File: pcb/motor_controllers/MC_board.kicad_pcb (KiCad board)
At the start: 2 copper layers, 21 parts, among them U1 Teensy3.2

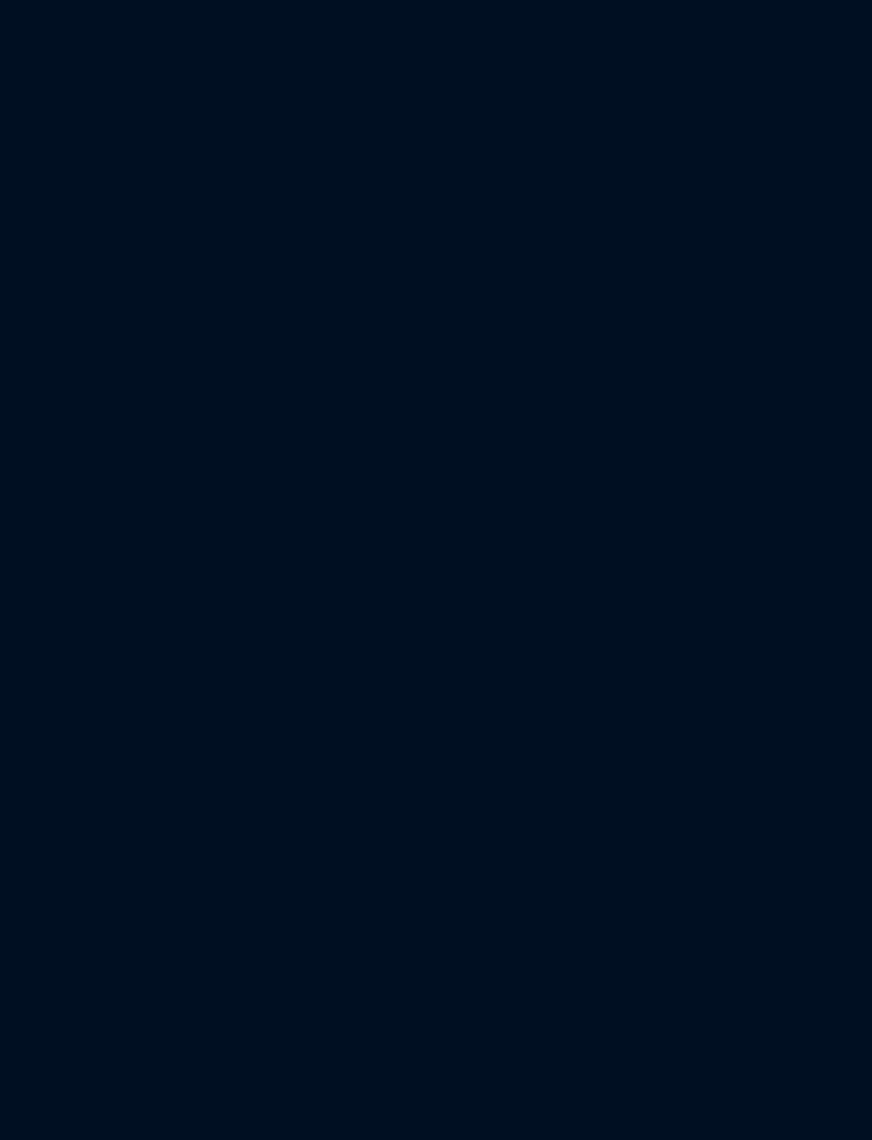
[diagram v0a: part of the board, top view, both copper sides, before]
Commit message: Added analog output RJ45 and audio amplifier symbol.
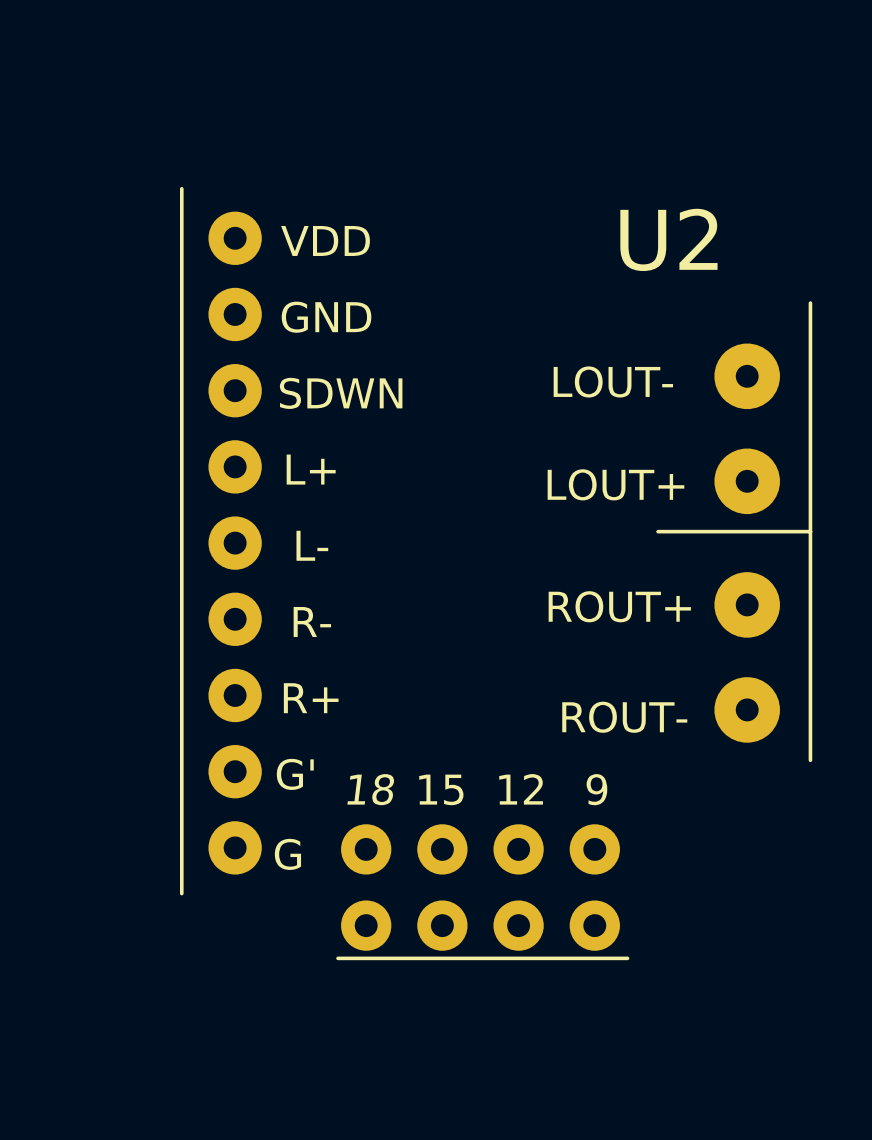
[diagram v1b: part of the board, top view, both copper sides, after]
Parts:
- added U2: MAX98306, spatialsparrow:MAX98306, F.Cu at (149.9, 83.8)
- 5V1: value Barrel_Jack -> 5V
- 9V1: value Barrel_Jack -> 9V
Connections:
- 9V1 pad 1: Net-(9V1-Pad1) -> +9V
- 9V1 pad 2: Net-(9V1-Pad2) -> GND
- C1 pad 1: Net-(9V1-Pad1) -> +9V
- C1 pad 2: Net-(9V1-Pad2) -> GND
- MC-LeverL1 pad 1: Net-(5V1-Pad2) -> GND
- MC-LeverL1 pad 14: Net-(5V1-Pad1) -> +5V
- MC-LeverL1 pad 7: Net-(9V1-Pad2) -> GND
- MC-LeverL1 pad 8: Net-(9V1-Pad1) -> +9V
- MC-LeverR1 pad 1: Net-(5V1-Pad2) -> GND
- MC-LeverR1 pad 14: Net-(5V1-Pad1) -> +5V
- MC-LeverR1 pad 7: Net-(9V1-Pad2) -> GND
- MC-LeverR1 pad 8: Net-(9V1-Pad1) -> +9V
- MC-SpoutL1 pad 1: Net-(5V1-Pad2) -> GND
- MC-SpoutL1 pad 14: Net-(5V1-Pad1) -> +5V
- MC-SpoutL1 pad 7: Net-(9V1-Pad2) -> GND
- MC-SpoutL1 pad 8: Net-(9V1-Pad1) -> +9V
- MC-SpoutR1 pad 1: Net-(5V1-Pad2) -> GND
- MC-SpoutR1 pad 14: Net-(5V1-Pad1) -> +5V
- MC-SpoutR1 pad 7: Net-(9V1-Pad2) -> GND
- MC-SpoutR1 pad 8: Net-(9V1-Pad1) -> +9V
- U1 pad 1: Net-(U1-Pad1) -> GND
- U1 pad 32: Net-(U1-Pad32) -> GND
- U1 pad 33: Net-(U1-Pad33) -> +5V
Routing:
- net Net-(5V1-Pad1): track 1.19 -> 0.00 mm
- net +5V: track 0.00 -> 1.19 mm
- net GND: track 0.00 -> 0.94 mm
- net Net-(9V1-Pad2): track 0.54 -> 0.00 mm

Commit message: ran connections and did board layout
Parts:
- removed 5VGNDTEST1, 5VTEST1, 9VGNDTEST1, 9VTEST1: TestPoint, TestPoint:TestPoint_Plated_Hole_D5.0mm
- removed C2, C3, C4: 100 uF, Capacitor_THT:C_Rect_L7.2mm_W7.2mm_P5.00mm_FKS2_FKP2_MKS2_MKP2
- added 12V1: 12V, Connector_BarrelJack:BarrelJack_Horizontal, F.Cu at (115.6, 54.6)
- added J12V1: Screw_Terminal_01x02, teensey:TerminalBlock_TE_282825-2_1x02_P5.08mm_Horizontal, F.Cu at (108.0, 124.5)
- added J12V2: Screw_Terminal_01x02, teensey:TerminalBlock_TE_282825-2_1x02_P5.08mm_Horizontal, F.Cu at (68.6, 124.5)
- added J12V3: Screw_Terminal_01x02, teensey:TerminalBlock_TE_282825-2_1x02_P5.08mm_Horizontal, F.Cu at (81.3, 124.5)
- added J12V4: Screw_Terminal_01x02, teensey:TerminalBlock_TE_282825-2_1x02_P5.08mm_Horizontal, F.Cu at (94.0, 124.5)
- added J2: RJ45, teensey:RJ45_sparkfun, F.Cu at (113.0, 27.9)
- added J5V1: Screw_Terminal_01x02, teensey:TerminalBlock_TE_282825-2_1x02_P5.08mm_Horizontal, F.Cu at (55.9, 124.5)
- added J5V2: Screw_Terminal_01x02, teensey:TerminalBlock_TE_282825-2_1x02_P5.08mm_Horizontal, F.Cu at (43.2, 124.5)
- added J9V1: Screw_Terminal_01x02, teensey:TerminalBlock_TE_282825-2_1x02_P5.08mm_Horizontal, F.Cu at (29.2, 124.5)
- added SoundVisionL1: Screw_Terminal_01x06, teensey:TerminalBlock_TE_282825-6_1x06_P5.08mm_Horizontal, F.Cu at (26.7, 34.3)
- added SoundVisionR1: Screw_Terminal_01x06, teensey:TerminalBlock_TE_282825-6_1x06_P5.08mm_Horizontal, F.Cu at (27.9, 110.5)
- added sync_trigger_out1: Screw_Terminal_01x05, teensey:TerminalBlock_TE_282825-5_1x05_P5.08mm_Horizontal, F.Cu at (88.9, 91.4)
- HandleL-ToMotor1: renamed from LeverL-ToMotor1; footprint TerminalBlock_TE-Connectivity:TerminalBlock_TE_282825-4_1x04_P5.08mm_Horizontal -> teensey:TerminalBlock_TE_282825-4_1x04_P5.08mm_Horizontal
- HandleR-ToMotor1: renamed from LeverR-ToMotor1; footprint TerminalBlock_TE-Connectivity:TerminalBlock_TE_282825-4_1x04_P5.08mm_Horizontal -> teensey:TerminalBlock_TE_282825-4_1x04_P5.08mm_Horizontal
- SpoutL-ToMotor1, SpoutR-ToMotor1: footprint TerminalBlock_TE-Connectivity:TerminalBlock_TE_282825-4_1x04_P5.08mm_Horizontal -> teensey:TerminalBlock_TE_282825-4_1x04_P5.08mm_Horizontal
- ToHandleL1: renamed from FromZeros1; value Screw_Terminal_01x04 -> Screw_Terminal_01x05; footprint TerminalBlock_TE-Connectivity:TerminalBlock_TE_282825-4_1x04_P5.08mm_Horizontal -> teensey:TerminalBlock_TE_282825-5_1x05_P5.08mm_Horizontal
- ToHandleR1: renamed from FromTouch1; value Screw_Terminal_01x04 -> Screw_Terminal_01x05; footprint TerminalBlock_TE-Connectivity:TerminalBlock_TE_282825-4_1x04_P5.08mm_Horizontal -> teensey:TerminalBlock_TE_282825-5_1x05_P5.08mm_Horizontal
- moved ToHandleR1 108.6 mm to (27.9, 83.8), turned to 0 degrees
- moved HandleL-ToMotor1 105.2 mm to (26.7, 21.6), turned to 0 degrees
- moved SpoutL-ToMotor1 103.6 mm to (27.9, 47.0), turned to 0 degrees
- moved MC-SpoutL1 103.0 mm to (59.7, 16.5), turned to 0 degrees
- moved U2 74.5 mm to (81.3, 54.6)
- moved 9V1 74.0 mm to (115.6, 71.1), turned to 180 degrees
- moved MC-LeverL1 64.5 mm to (59.7, 41.9), turned to 0 degrees
- moved ToHandleL1 55.1 mm to (27.9, 59.7), turned to 0 degrees
- moved 5V1 54.8 mm to (115.6, 87.6), turned to 180 degrees
- moved SpoutR-ToMotor1 53.7 mm to (27.9, 96.5), turned to 0 degrees
- moved HandleR-ToMotor1 53.6 mm to (27.9, 73.7), turned to 0 degrees
- moved MC-SpoutR1 33.6 mm to (59.7, 94.0)
- moved MC-LeverR1 33.4 mm to (59.7, 67.3)
- moved C1 28.7 mm to (99.1, 100.3)
- moved U1 13.0 mm to (90.2, 34.3)
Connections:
- 5V1 pad 1: Net-(5V1-Pad1) -> +5V
- 5V1 pad 2: Net-(5V1-Pad2) -> GND
- ToHandleL1 pad 1: Net-(FromZeros1-Pad1) -> Net-(ToHandleL1-Pad1)
- ToHandleL1 pad 2: Net-(FromZeros1-Pad2) -> Net-(J2-Pad7)
- ToHandleL1 pad 3: Net-(FromZeros1-Pad3) -> GND
- ToHandleL1 pad 4: Net-(FromZeros1-Pad4) -> Net-(ToHandleL1-Pad4)
- ToHandleR1 pad 1: Net-(FromTouch1-Pad1) -> Net-(ToHandleR1-Pad1)
- ToHandleR1 pad 2: Net-(FromTouch1-Pad2) -> Net-(J2-Pad8)
- ToHandleR1 pad 3: Net-(FromTouch1-Pad3) -> GND
- ToHandleR1 pad 4: Net-(FromTouch1-Pad4) -> Net-(ToHandleR1-Pad4)
- U1 pad 10: Net-(FromZeros1-Pad1) -> Net-(FromTouch1-Pad4)
- U1 pad 11: Net-(MC-LeverL1-Pad9) -> Net-(MC-LeverL1-Pad15)
- U1 pad 12: Net-(MC-LeverL1-Pad15) -> Net-(MC-LeverL1-Pad16)
- U1 pad 22: Net-(FromTouch1-Pad4) -> Net-(FromZeros1-Pad1)
- U1 pad 23: Net-(FromTouch1-Pad3) -> Net-(FromTouch1-Pad1)
- U1 pad 29: Net-(FromTouch1-Pad2) -> Net-(SoundVision1-Pad1)
- U1 pad 30: Net-(FromTouch1-Pad1) -> Net-(SoundVision2-Pad1)
- U1 pad 7: Net-(FromZeros1-Pad4) -> Net-(SoundVision1-Pad4)
- U1 pad 8: Net-(FromZeros1-Pad3) -> Net-(SoundVision2-Pad4)
- U1 pad 9: Net-(FromZeros1-Pad2) -> Net-(FromZeros1-Pad4)
- U2 pad 1: +5V -> Net-(U2-Pad1)
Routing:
- net Net-(FromZeros1-Pad4): track 7.18 -> 0.00 mm
- net Net-(FromZeros1-Pad3): track 3.59 -> 0.00 mm
- net Net-(FromZeros1-Pad1): track 3.59 -> 0.00 mm
- net Net-(HandleL-ToMotor1-Pad4): track 1.13 -> 0.00 mm
- net Net-(SoundVisionL1-Pad3): track 0.00 -> 1.13 mm
- net Net-(HandleL-ToMotor1-Pad1): track 1.03 -> 0.00 mm
- net Net-(LeverL-ToMotor1-Pad1): track 0.00 -> 1.03 mm
- net +9V: track 0.00 -> 0.79 mm
- net +5V: track 1.19 -> 0.40 mm
